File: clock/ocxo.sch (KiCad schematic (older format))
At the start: 42 parts, among them Q201 MMBT3904, U201 PCA9306, U202 DAC8830, U203 LMV722, U204 LTC2990, U205 LP3853, U207 NC7SZ125, Y202 CX210

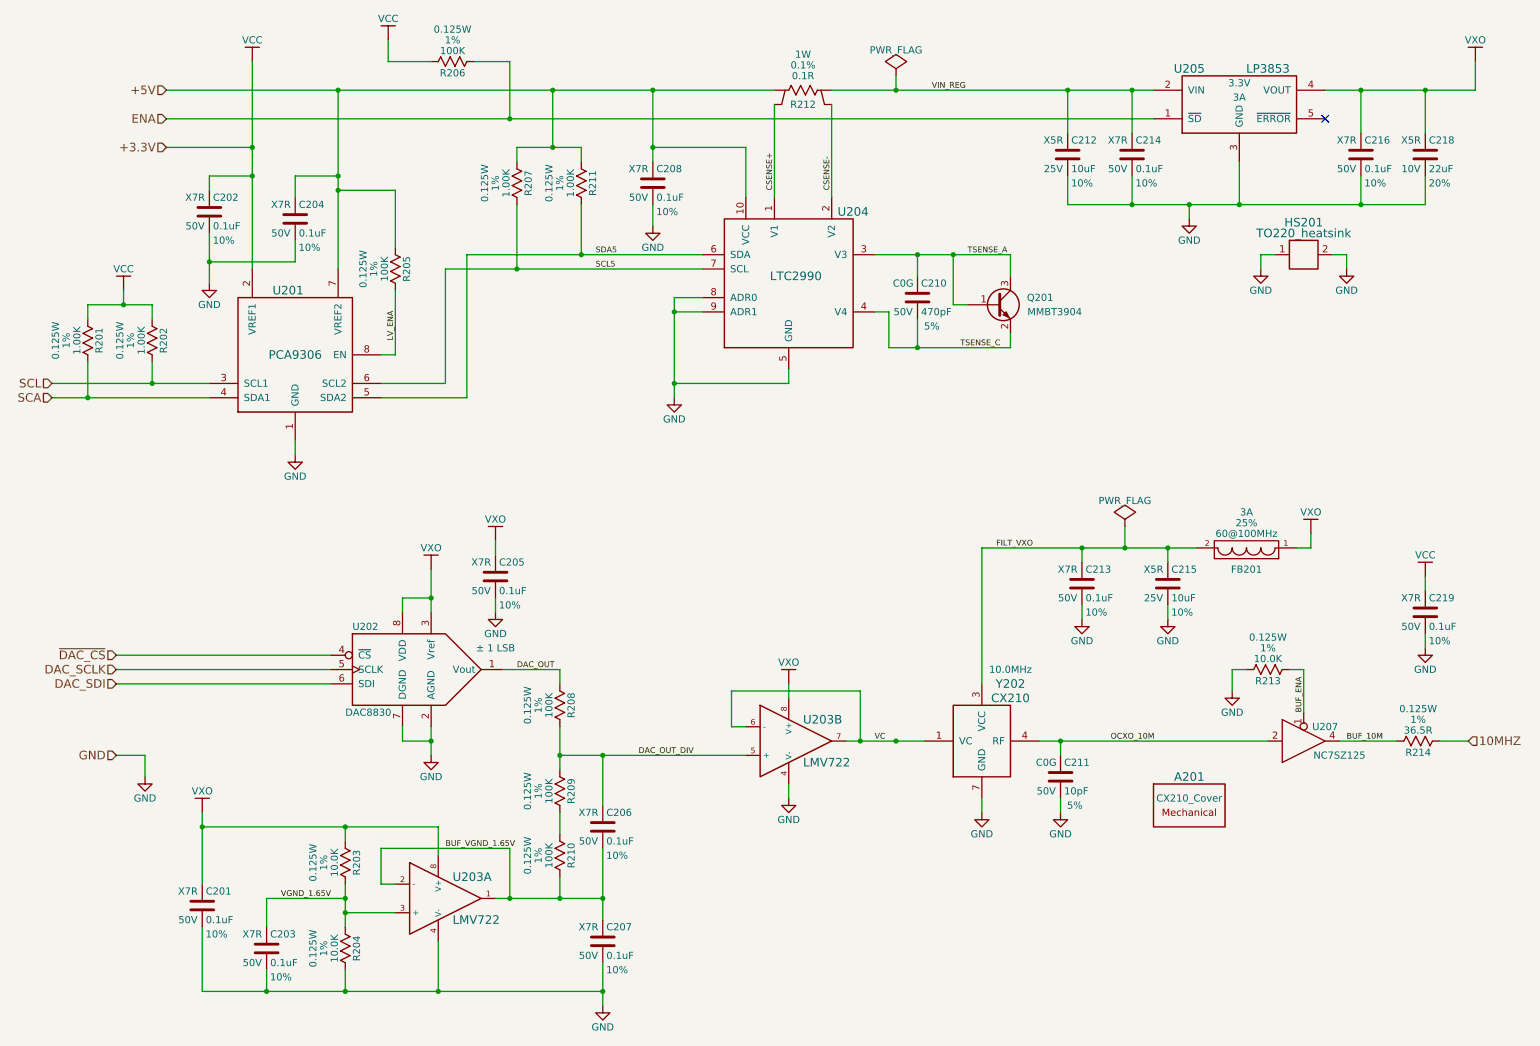
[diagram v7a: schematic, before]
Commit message: Add second capacitor to 3V LDO input. Add series resistor to LDO enable.
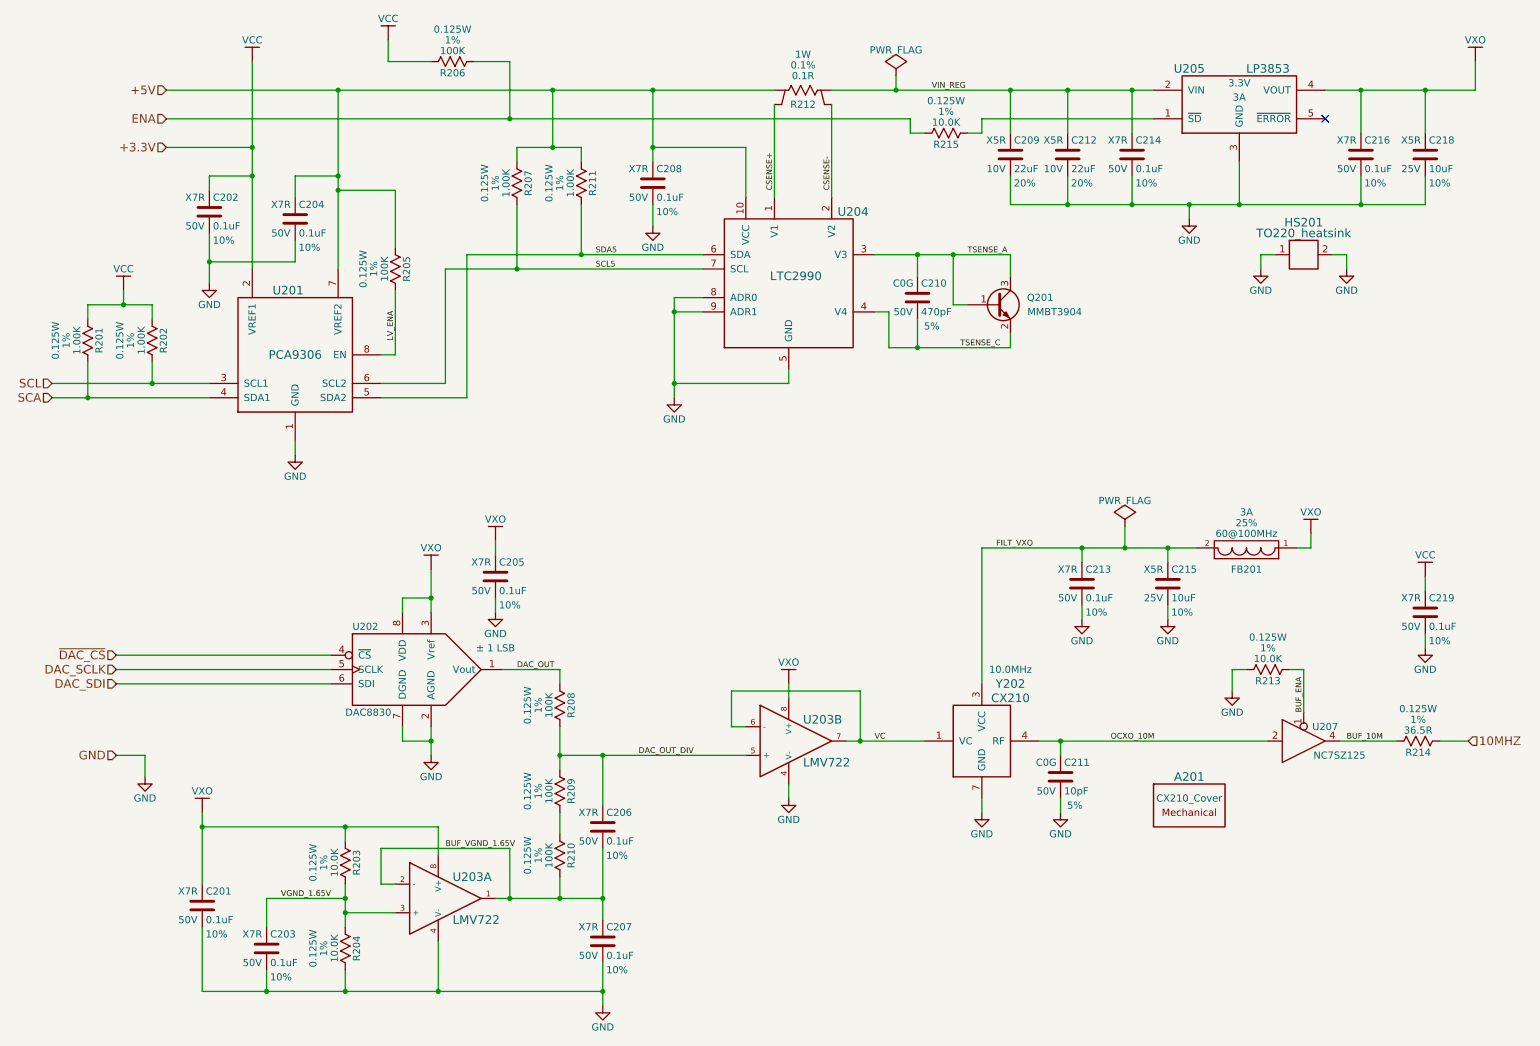
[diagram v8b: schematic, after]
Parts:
- added C209: 22uF, Capacitors_SMD:C_1206_HandSoldering, symbol C
- added R215: 10.0K, Resistors_SMD:R_0805_HandSoldering, symbol R_local
- C212: value 10uF -> 22uF; PartNum C3216X5R1E106K160AB -> C3216X5R1A226M160AC; Tolerance 10% -> 20%; Voltage 25V -> 10V
- C218: value 22uF -> 10uF; PartNum C3216X5R1A226M160AC -> C3216X5R1E106K160AB; Tolerance 20% -> 10%; Voltage 10V -> 25V
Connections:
- net ENA: now also R215.2; no longer U205.1 (~SD~)
- net GND: now also C209.2
- net VIN_REG: now also C209.1
- new net: R215.1, U205.1 (~SD~)
